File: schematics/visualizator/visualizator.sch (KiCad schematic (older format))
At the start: 20 parts, among them J1 5V, J2 WS2812, J3 Audio, SW1 COLOR, SW2 PATTERN, U1 ATmega328-16PU, Y1 16MHz

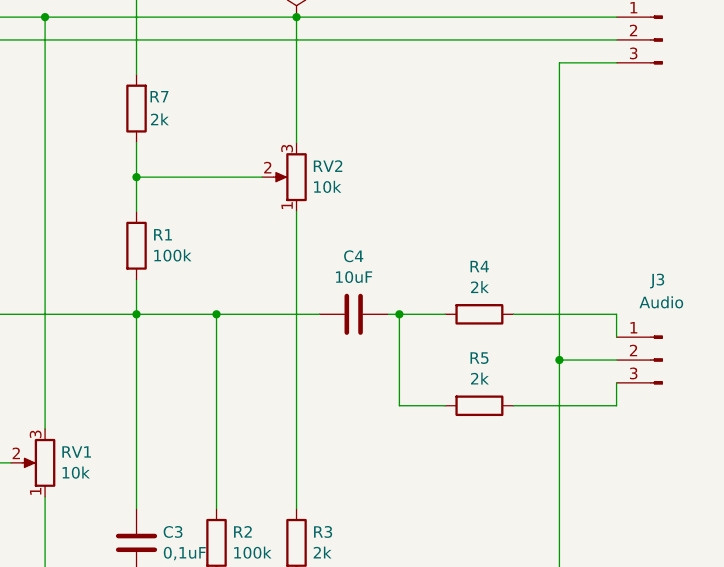
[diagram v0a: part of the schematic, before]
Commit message: Changed reistors
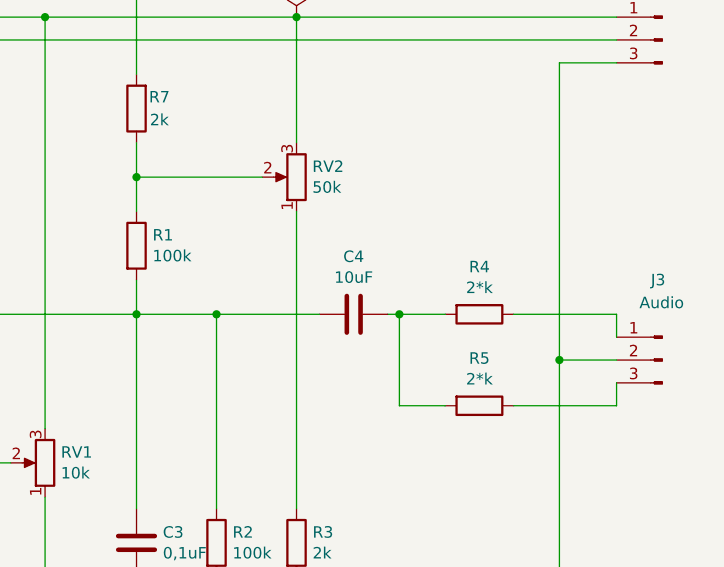
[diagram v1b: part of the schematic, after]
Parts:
- R4, R5: value 2k -> 2*k
- RV2: value 10k -> 50k
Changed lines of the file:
@@
 P 7750 2400
 F 0 "RV2" H 7681 2354 50  0000 R CNN
-F 1 "10k" H 7681 2445 50  0000 R CNN
+F 1 "50k" H 7681 2445 50  0000 R CNN
 F 2 "Connector_Wire:SolderWirePad_1x03_P3.175mm_Drill0.8mm" H 7750 2400 50  0001 C CNN
 F 3 "~" H 7750 2400 50  0001 C CNN
@@
 P 8550 3000
 F 0 "R4" V 8343 3000 50  0000 C CNN
-F 1 "2k" V 8434 3000 50  0000 C CNN
+F 1 "2*k" V 8434 3000 50  0000 C CNN
 F 2 "Resistor_THT:R_Axial_DIN0207_L6.3mm_D2.5mm_P10.16mm_Horizontal" V 8480 3000 50  0001 C CNN
 F 3 "~" H 8550 3000 50  0001 C CNN
@@
 P 8550 3400
 F 0 "R5" V 8343 3400 50  0000 C CNN
-F 1 "2k" V 8434 3400 50  0000 C CNN
+F 1 "2*k" V 8434 3400 50  0000 C CNN
 F 2 "Resistor_THT:R_Axial_DIN0207_L6.3mm_D2.5mm_P10.16mm_Horizontal" V 8480 3400 50  0001 C CNN
 F 3 "~" H 8550 3400 50  0001 C CNN

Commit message: PCBs updated
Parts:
- C3: footprint Capacitor_THT:C_Rect_L13.5mm_W4.0mm_P10.00mm_FKS3_FKP3_MKS4 -> Capacitor_THT:C_Disc_D4.3mm_W1.9mm_P5.00mm
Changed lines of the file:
@@
 F 0 "C3" H 7165 4046 50  0000 L CNN
 F 1 "0,1uF" H 7165 3955 50  0000 L CNN
-F 2 "Capacitor_THT:C_Rect_L13.5mm_W4.0mm_P10.00mm_FKS3_FKP3_MKS4" H 7088 3850 50  0001 C CNN
+F 2 "Capacitor_THT:C_Disc_D4.3mm_W1.9mm_P5.00mm" H 7088 3850 50  0001 C CNN
 F 3 "~" H 7050 4000 50  0001 C CNN
 	1    7050 4000
